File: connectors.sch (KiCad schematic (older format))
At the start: 43 parts, among them J12 20021121-00010C4LF, J13 70543-0001, J14 70543-0001, J15 70543-0001, J16 70543-0001, J17 70543-0001, J18 70543-0001, J19 70543-0001, J20 70543-0001, J21 70543-0003, J22 70543-0002, J23 70543-0002, J24 70543-0002, J25 Conn_02x20_Odd_Even

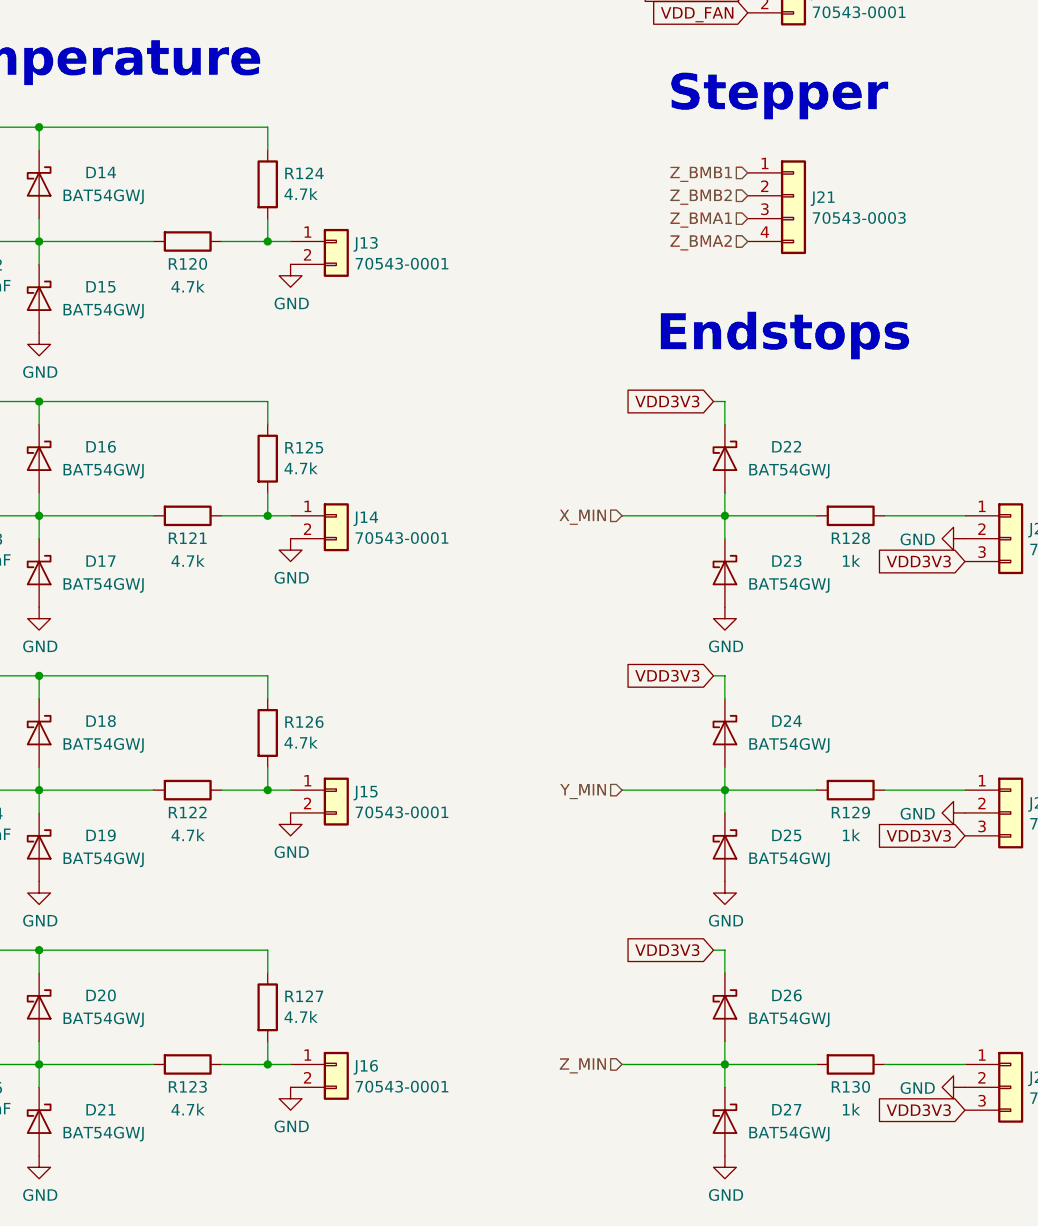
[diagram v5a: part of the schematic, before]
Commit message: Add PD resistor to BOOT PIN
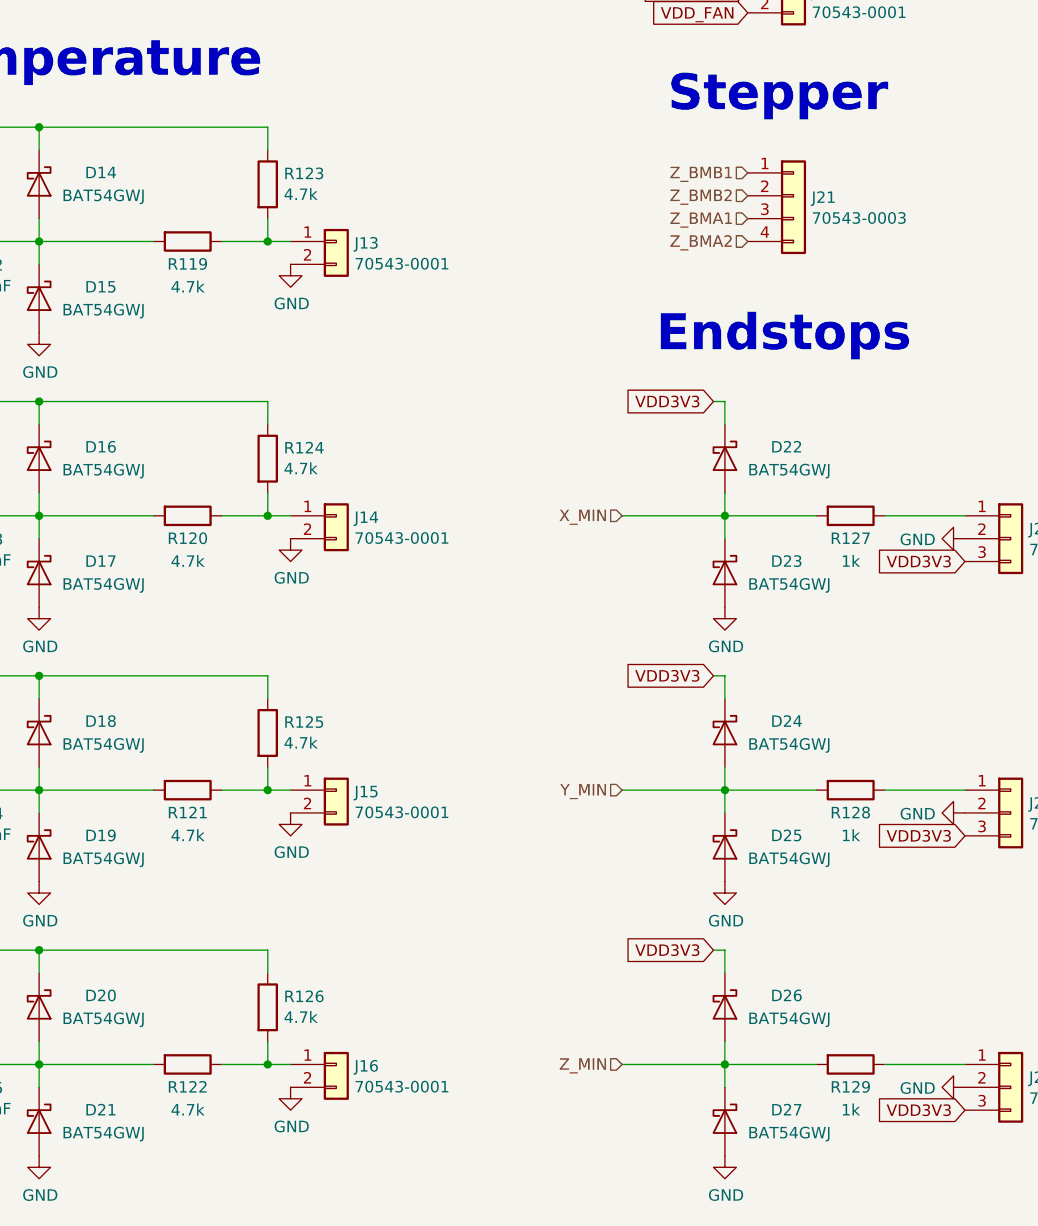
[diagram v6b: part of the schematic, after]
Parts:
- renumbered R120 to R119, R121 to R120, R122 to R121, R123 to R122, R124 to R123, R125 to R124, R126 to R125, R127 to R126, R128 to R127, R129 to R128, R130 to R129
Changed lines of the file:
@@
 EESchema Schematic File Version 4
 LIBS:heteromycin-cache
-EELAYER 29 0
+EELAYER 26 0
 EELAYER END
 $Descr A4 11693 8268
@@
 TEMP1
 $Comp
-L Device:R R120
+L Device:R R119
 U 1 1 5B1719A1
 P 2150 3300
-F 0 "R120" V 2250 3300 50  0000 C CNN
+F 0 "R119" V 2250 3300 50  0000 C CNN
 F 1 "4.7k" V 2350 3300 50  0000 C CNN
 F 2 "Resistor_SMD:R_0603_1608Metric" V 2080 3300 50  0001 C CNN
@@
 $EndComp
 $Comp
-L Device:R R124
+L Device:R R123
 U 1 1 5B1719A8
 P 2500 3050
-F 0 "R124" H 2570 3096 50  0000 L CNN
+F 0 "R123" H 2570 3096 50  0000 L CNN
 F 1 "4.7k" H 2570 3005 50  0000 L CNN
 F 2 "Resistor_SMD:R_0603_1608Metric" V 2430 3050 50  0001 C CNN
@@
 VDD_FAN
 $Comp
-L Device:R R128
+L Device:R R127
 U 1 1 5B40FD8A
 P 5050 4500
-F 0 "R128" V 5150 4500 50  0000 C CNN
+F 0 "R127" V 5150 4500 50  0000 C CNN
 F 1 "1k" V 5250 4500 50  0000 C CNN
 F 2 "Resistor_SMD:R_0603_1608Metric" V 4980 4500 50  0001 C CNN
@@
 	4500 4500 4900 4500
 $Comp
-L Device:R R129
+L Device:R R128
 U 1 1 5B453619
 P 5050 5700
-F 0 "R129" V 5150 5700 50  0000 C CNN
+F 0 "R128" V 5150 5700 50  0000 C CNN
 F 1 "1k" V 5250 5700 50  0000 C CNN
 F 2 "Resistor_SMD:R_0603_1608Metric" V 4980 5700 50  0001 C CNN
@@
 	4500 5700 4900 5700
 $Comp
-L Device:R R130
+L Device:R R129
 U 1 1 5B45771E
 P 5050 6900
-F 0 "R130" V 5150 6900 50  0000 C CNN
+F 0 "R129" V 5150 6900 50  0000 C CNN
 F 1 "1k" V 5250 6900 50  0000 C CNN
 F 2 "Resistor_SMD:R_0603_1608Metric" V 4980 6900 50  0001 C CNN
@@
 Connection ~ 2500 3300
 $Comp
-L Device:R R121
+L Device:R R120
 U 1 1 5B5657F4
 P 2150 4500
-F 0 "R121" V 2250 4500 50  0000 C CNN
+F 0 "R120" V 2250 4500 50  0000 C CNN
 F 1 "4.7k" V 2350 4500 50  0000 C CNN
 F 2 "Resistor_SMD:R_0603_1608Metric" V 2080 4500 50  0001 C CNN
@@
 $EndComp
 $Comp
-L Device:R R125
+L Device:R R124
 U 1 1 5B5657FB
 P 2500 4250
-F 0 "R125" H 2570 4296 50  0000 L CNN
+F 0 "R124" H 2570 4296 50  0000 L CNN
 F 1 "4.7k" H 2570 4205 50  0000 L CNN
 F 2 "Resistor_SMD:R_0603_1608Metric" V 2430 4250 50  0001 C CNN
@@
 Connection ~ 2500 4500
 $Comp
-L Device:R R122
+L Device:R R121
 U 1 1 5B57C5BA
 P 2150 5700
-F 0 "R122" V 2250 5700 50  0000 C CNN
+F 0 "R121" V 2250 5700 50  0000 C CNN
 F 1 "4.7k" V 2350 5700 50  0000 C CNN
 F 2 "Resistor_SMD:R_0603_1608Metric" V 2080 5700 50  0001 C CNN
@@
 $EndComp
 $Comp
-L Device:R R126
+L Device:R R125
 U 1 1 5B57C5C1
 P 2500 5450
-F 0 "R126" H 2570 5496 50  0000 L CNN
+F 0 "R125" H 2570 5496 50  0000 L CNN
 F 1 "4.7k" H 2570 5405 50  0000 L CNN
 F 2 "Resistor_SMD:R_0603_1608Metric" V 2430 5450 50  0001 C CNN
@@
 $EndComp
 $Comp
-L Device:R R123
+L Device:R R122
 U 1 1 5BC983A7
 P 2150 6900
-F 0 "R123" V 2250 6900 50  0000 C CNN
+F 0 "R122" V 2250 6900 50  0000 C CNN
 F 1 "4.7k" V 2350 6900 50  0000 C CNN
 F 2 "Resistor_SMD:R_0603_1608Metric" V 2080 6900 50  0001 C CNN
@@
 $EndComp
 $Comp
-L Device:R R127
+L Device:R R126
 U 1 1 5BC983AE
 P 2500 6650
-F 0 "R127" H 2570 6696 50  0000 L CNN
+F 0 "R126" H 2570 6696 50  0000 L CNN
 F 1 "4.7k" H 2570 6605 50  0000 L CNN
 F 2 "Resistor_SMD:R_0603_1608Metric" V 2430 6650 50  0001 C CNN
